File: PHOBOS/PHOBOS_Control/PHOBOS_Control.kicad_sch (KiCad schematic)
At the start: 83 parts, among them J1 Screw_Terminal_01x02, J2 Conn_01x06, J3 Conn_Coaxial, J4 USB Boot, J5 DE9_Pins_MountingHoles, J6 USB4056-03-A_REVA2, J7 SMA-J-P-GF-RA-SM1, SW4 KMR211GLFS, U1 SX1280IMLTRT, U2 TLV9351IDCKR, U3 W25Q128JVSIQ, U4 NCP1117-3.3_SOT223, U5 RP2040, U6 TLV9351IDCKR, U7 TLV9351IDCKR, U8 TLV9351IDCKR, Y1 ABM8-272-T3, Y2 C1E-52.000-10-1012-X-M

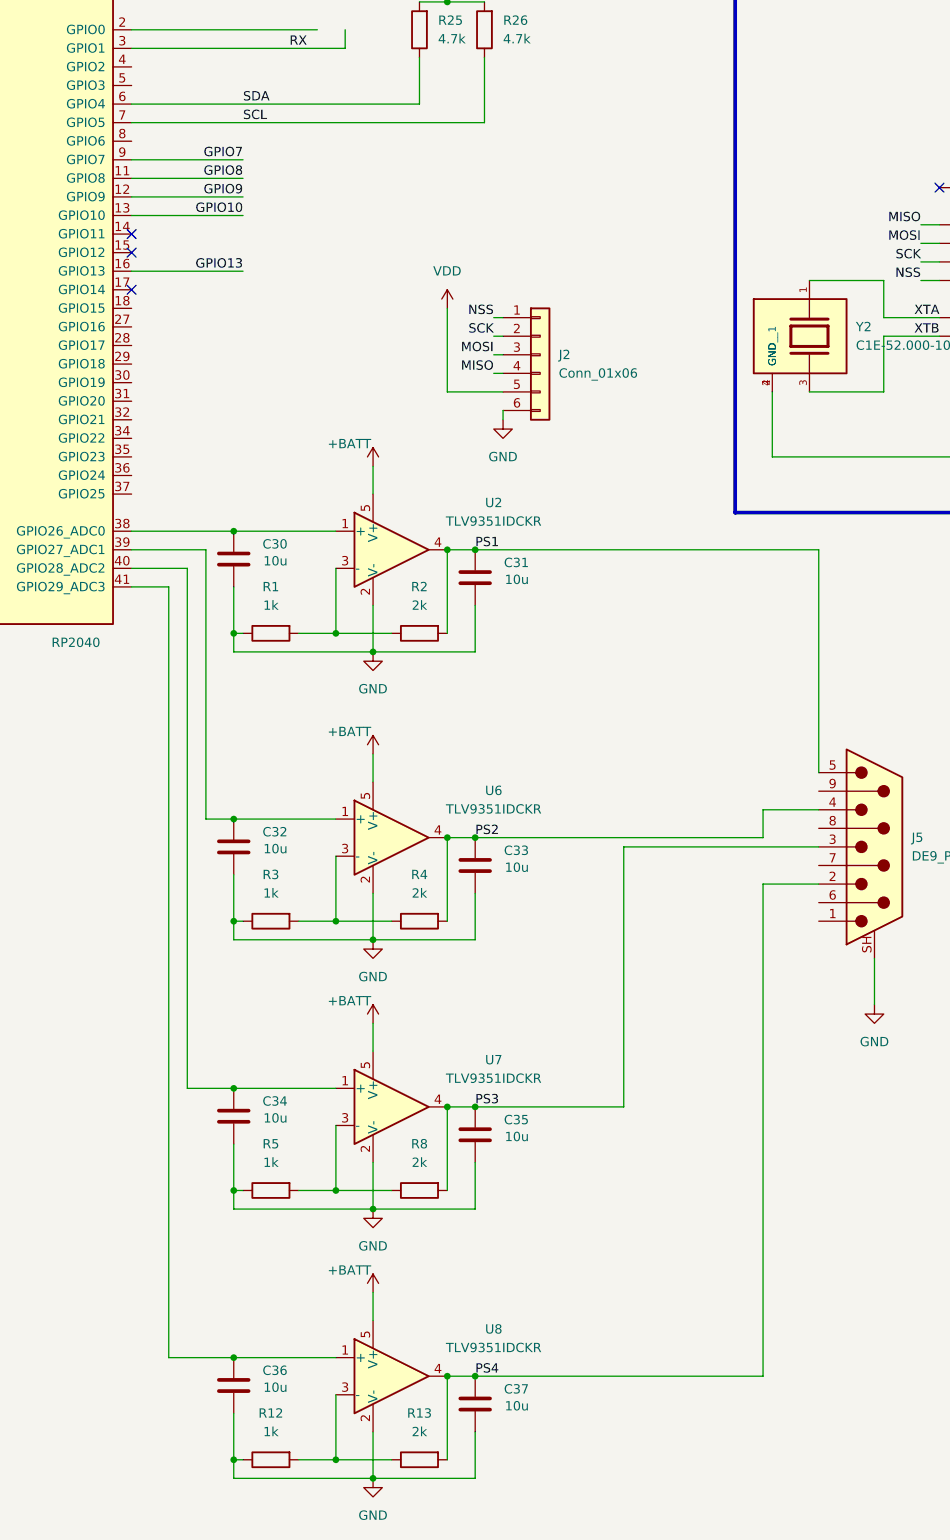
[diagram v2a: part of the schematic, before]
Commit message: op amp pins moved to random gpio
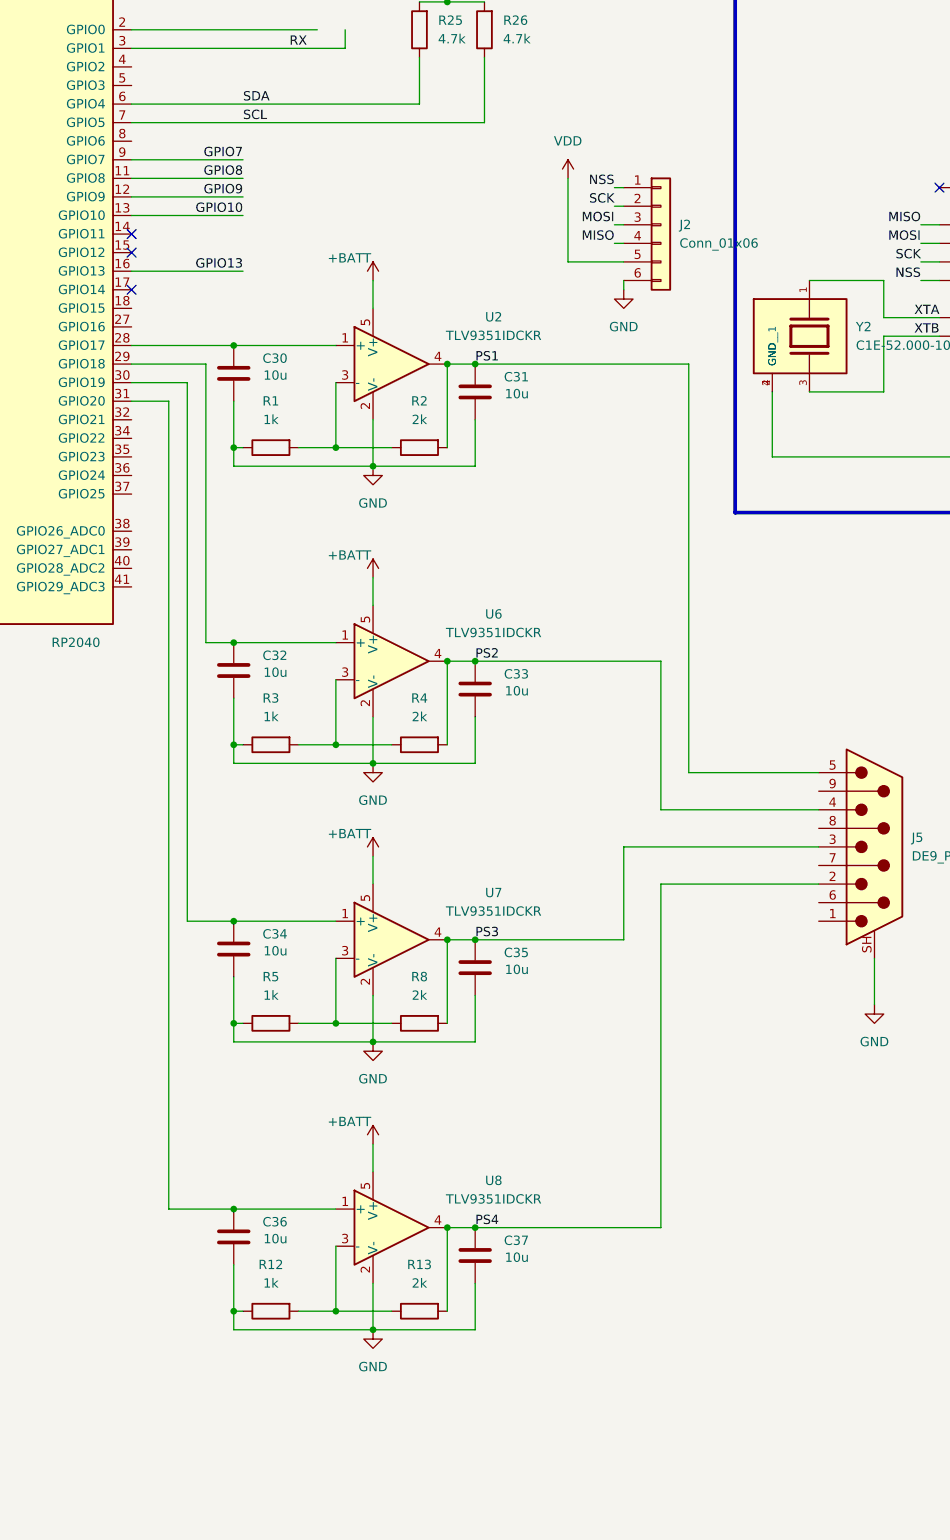
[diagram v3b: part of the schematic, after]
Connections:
- net at C32.1, U6.1 (+): now also U5.29 (GPIO18); no longer U5.39 (GPIO27_ADC1)
- net at U5.28 (GPIO17): now also C30.1, U2.1 (+)
- net at U5.30 (GPIO19): now also C34.1, U7.1 (+)
- net at U5.31 (GPIO20): now also C36.1, U8.1 (+)
- now unconnected: U5.38 (GPIO26_ADC0), U5.40 (GPIO28_ADC2), U5.41 (GPIO29_ADC3)
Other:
- moved on the sheet: C30, C31, C32, C33, C34, C35, C36, C37, J2, R1, R12, R13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

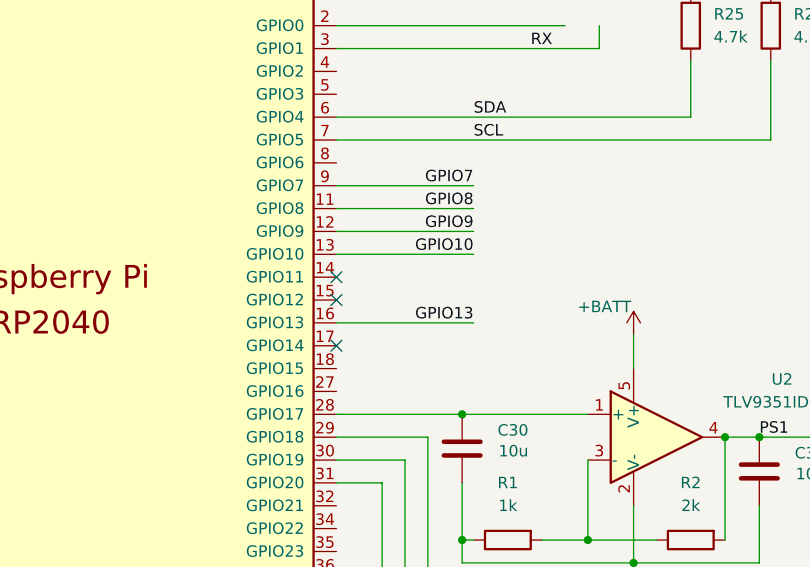
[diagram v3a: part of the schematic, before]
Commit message: SPI1 connected
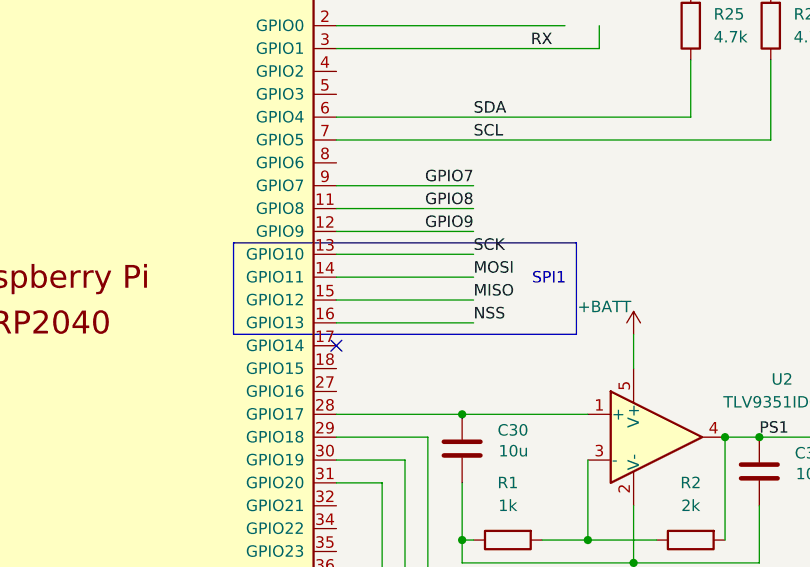
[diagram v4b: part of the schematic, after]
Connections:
- net GPIO10 is gone; now on net SCK: U5.13 (GPIO10)
- net GPIO13 is gone; now on net NSS: U5.16 (GPIO13)
- net MISO: now also U5.15 (GPIO12)
- net MOSI: now also U5.14 (GPIO11)
- no-connect marks 14 -> 12
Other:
- note added: "SPI1"
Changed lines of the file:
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@@
 	)
 	(rectangle
+		(start 307.34 213.36)
+		(end 345.44 223.52)
+		(stroke
+			(width 0)
+			(type default)
+		)
+		(fill
+			(type none)
+		)
+	)
+	(rectangle
 		(start 99.06 83.82)
 		(end 238.76 165.735)
@@
 		)
 	)
+	(text "SPI1"
+		(exclude_from_sim no)
+		(at 342.392 217.424 0)
+		(effects
+			(font
+				(size 1.27 1.27)
+			)
+		)
+	)
 	(text "I2C PU"
 		(exclude_from_sim no)
@@
 	)
 	(no_connect
-		(at 318.77 217.17)
-	)
-	(no_connect
 		(at 110.49 127)
 	)
@@
 	)
 	(no_connect
-		(at 318.77 219.71)
-	)
-	(no_connect
 		(at 146.05 111.76)
 	)
@@
 	(wire
 		(pts
+			(xy 318.77 217.17) (xy 334.01 217.17)
+		)
+		(stroke
+			(width 0)
+			(type default)
+		)
+	)
+	(wire
+		(pts
 			(xy 367.03 149.86) (xy 367.03 151.13)
 		)
@@
 	(wire
 		(pts
+			(xy 318.77 219.71) (xy 334.01 219.71)
+		)
+		(stroke
+			(width 0)
+			(type default)
+		)
+	)
+	(wire
+		(pts
 			(xy 346.71 246.38) (xy 354.33 246.38)
 		)
@@
 		)
 	)
-	(label "GPIO10"
-		(at 334.01 214.63 180)
+	(label "MISO"
+		(at 334.01 219.71 0)
 		(effects
 			(font
 				(size 1.27 1.27)
 			)
-			(justify right bottom)
+			(justify left bottom)
 		)
 	)
@@
 		)
 	)
+	(label "MOSI"
+		(at 334.01 217.17 0)
+		(effects
+			(font
+				(size 1.27 1.27)
+			)
+			(justify left bottom)
+		)
+	)
 	(label "~{USB_BOOT}"
 		(at 184.15 189.23 180)
@@
 		)
 	)
+	(label "SCK"
+		(at 334.01 214.63 0)
+		(effects
+			(font
+				(size 1.27 1.27)
+			)
+			(justify left bottom)
+		)
+	)
 	(label "QSPI_SD3"
 		(at 162.56 201.93 180)
@@
 	)
 	(label "NSS"
-		(at 384.81 210.82 180)
+		(at 334.01 222.25 0)
 		(effects
 			(font
 				(size 1.27 1.27)
 			)
-			(justify right bottom)
+			(justify left bottom)
 		)
 	)
-	(label "GPIO13"
-		(at 334.01 222.25 180)
+	(label "NSS"
+		(at 384.81 210.82 180)
 		(effects
 			(font

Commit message: power section re routed
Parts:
- removed J7: SMA-J-P-GF-RA-SM1, SMA-J-P-GF-RA-SM1:SAMTEC_SMA-J-P-GF-RA-SM1, symbol SMA_J_P_GF_RA_SM1:SMA-J-P-GF-RA-SM1
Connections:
- net GND: now also C3.1, C8.1; no longer C3.2, C8.2
- net VIN: now also C3.2, C8.2; no longer C3.1, C8.1
- no-connect marks 12 -> 34
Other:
- note added: "USB/Power"
- note removed: "USB_In and Regulator"
- moved on the sheet: C12, C13, C14, C15, C16, C3, C8, D1, D5, J1, R9, U4
